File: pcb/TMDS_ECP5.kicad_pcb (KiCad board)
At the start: 4 copper layers, 44 x 38 mm, 39 parts, among them J1 HDMI_A_1.4, J2 Conn_02x16_Odd_Even, J3 Conn_01x03

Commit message: revised pcb layout
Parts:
- moved C9 27.7 mm to (126.5, 82.2)
- moved C10 27.4 mm to (128.0, 82.2)
- moved R5 7.86 mm to (107.7, 81.5)
- moved R6 7.41 mm to (107.7, 83.0)
- moved R7 6.45 mm to (110.7, 81.5)
- moved R8 6.01 mm to (110.7, 83.0)
- moved R9 3.19 mm to (113.2, 81.5)
- moved R10 3.01 mm to (113.1, 82.5)
- moved R13 3.00 mm to (118.0, 81.0)
- moved R14 2.63 mm to (118.0, 82.4)
- moved R2 2.53 mm to (133.5, 81.5)
- moved R1 2.20 mm to (133.5, 83.0)
- moved R12 2.08 mm to (115.7, 82.5)
- moved R11 2.07 mm to (115.7, 81.5)
- moved R3 1.53 mm to (136.0, 83.0), turned to 180 degrees
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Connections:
- J2 pad 2: +3V3 -> unconnected-(J2-Pin_2-Pad2)
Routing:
- net +2V5: track 90.7 -> 56.4 mm, vias 5 -> 4
- net GND: track 42.2 -> 10.6 mm, vias 17 -> 8
- net +3V3: track 72.5 -> 50.8 mm
- net /d0_1v25_N: track 42.8 -> 34.2 mm
- net /d0_1v25_P: track 43.0 -> 37.0 mm
- net /clk_1v25_N: track 28.0 -> 22.6 mm
- net /d1_1v25_N: track 35.8 -> 30.8 mm
- net /clk_1v25_P: track 28.3 -> 25.6 mm
- net /d2_1v25_P: track 30.1 -> 32.0 mm
- net /d1_1v25_P: track 35.7 -> 34.0 mm
- net /d2_1v25_N: track 30.0 -> 28.5 mm
- net /d0_3v3_P: track 6.63 -> 6.10 mm

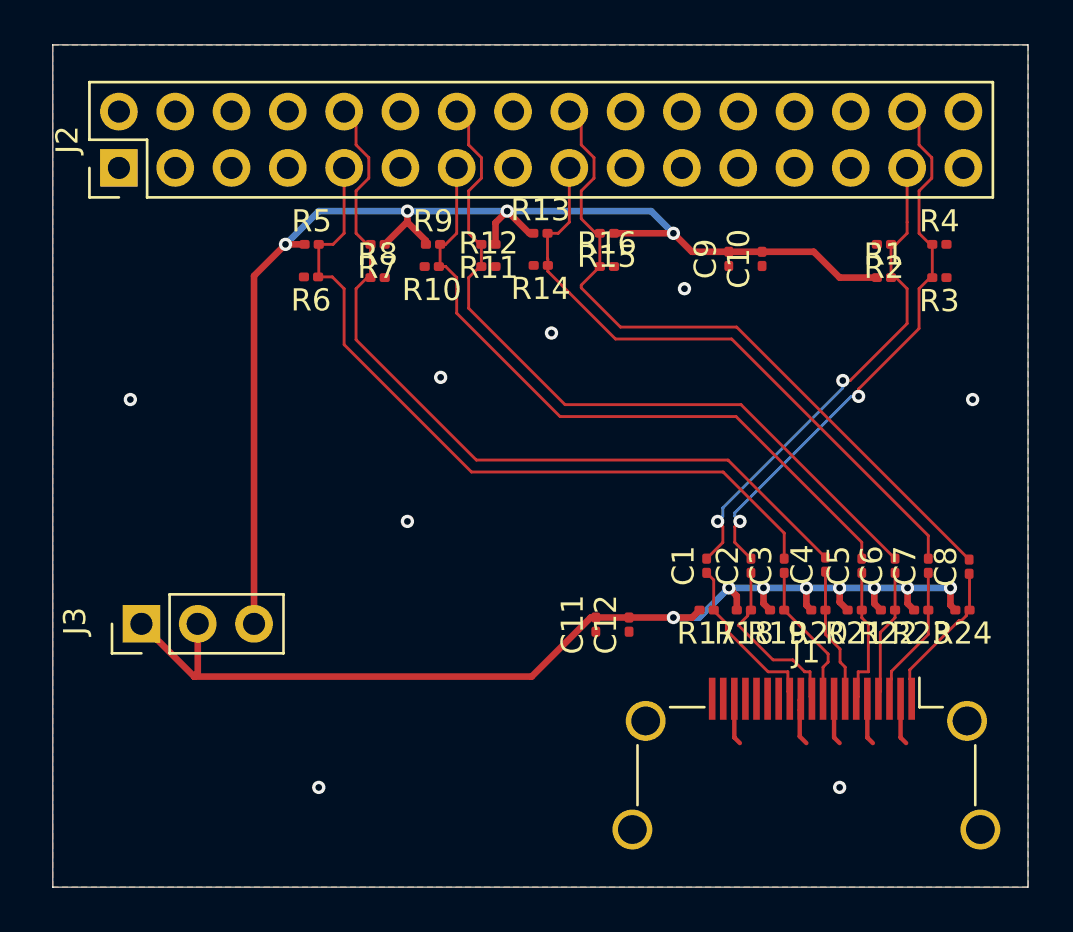
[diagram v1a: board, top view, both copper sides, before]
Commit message: length matching
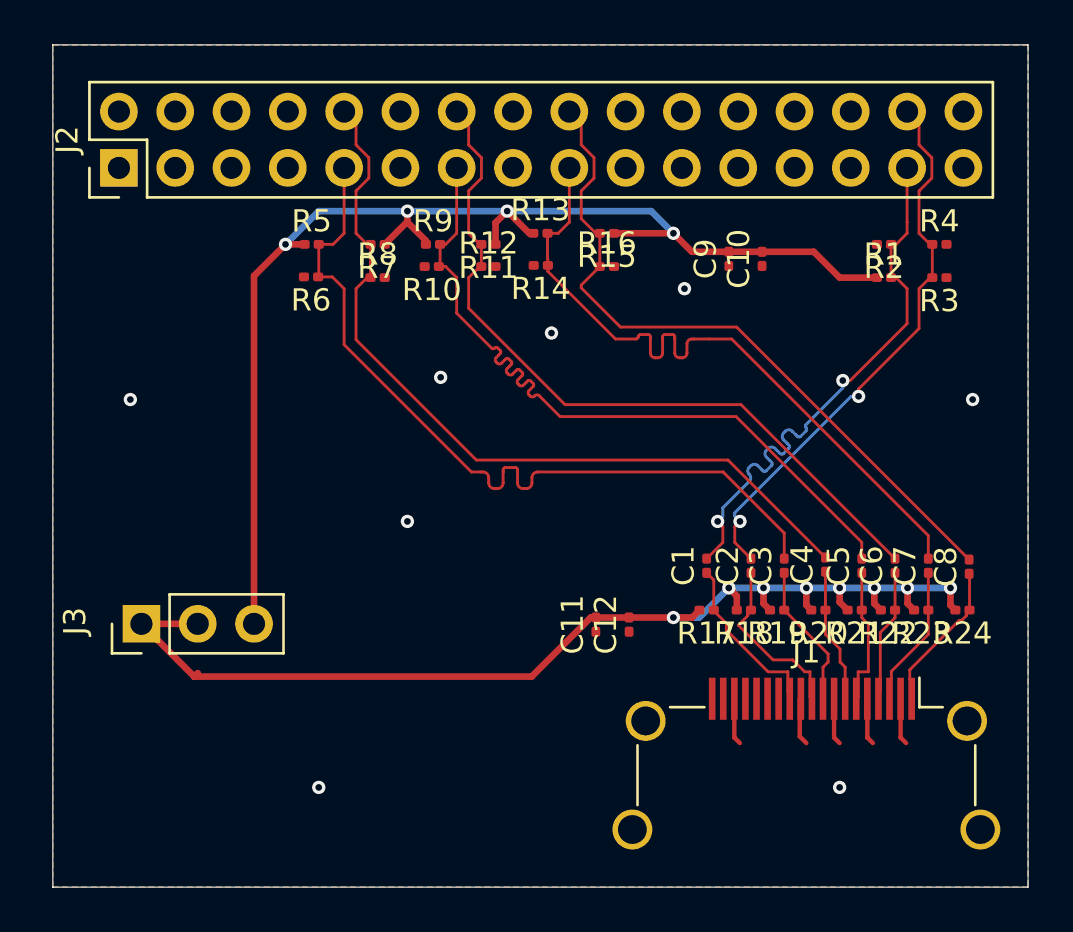
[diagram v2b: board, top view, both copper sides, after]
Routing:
- net /d2_1v25_N: track 28.5 -> 32.0 mm
- net /d1_1v25_N: track 30.8 -> 33.8 mm
- net /clk_1v25_N: track 22.6 -> 25.5 mm
- net /d0_1v25_N: track 34.2 -> 36.8 mm

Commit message: silk screen cleanup
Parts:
- C11: value 100n -> 100nF
- C12: value 1u -> 1uF
- R8: value 10k -> 10kohm
- renumbered C8 to 100nF, C9 to 100nF, R4 to 10kohm, C10 to 1uF, R17 to 50ohm, J1 to HDMI, J2 to J33, J3 to JP11

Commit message: clean silkscren; trace repair; DRC pass
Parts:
- R8: value 10kohm -> 10k
- renumbered 10kohm to 10k, 50ohm to 50
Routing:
- net +2V5: track 56.4 -> 71.9 mm, vias 4 -> 5
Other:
- board text added: "VsyncExtractor v0.1 Ownasaurus ReverendGumby"
